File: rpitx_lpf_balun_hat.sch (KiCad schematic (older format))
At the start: 5 parts, among them P1 Conn_02x20_Odd_Even

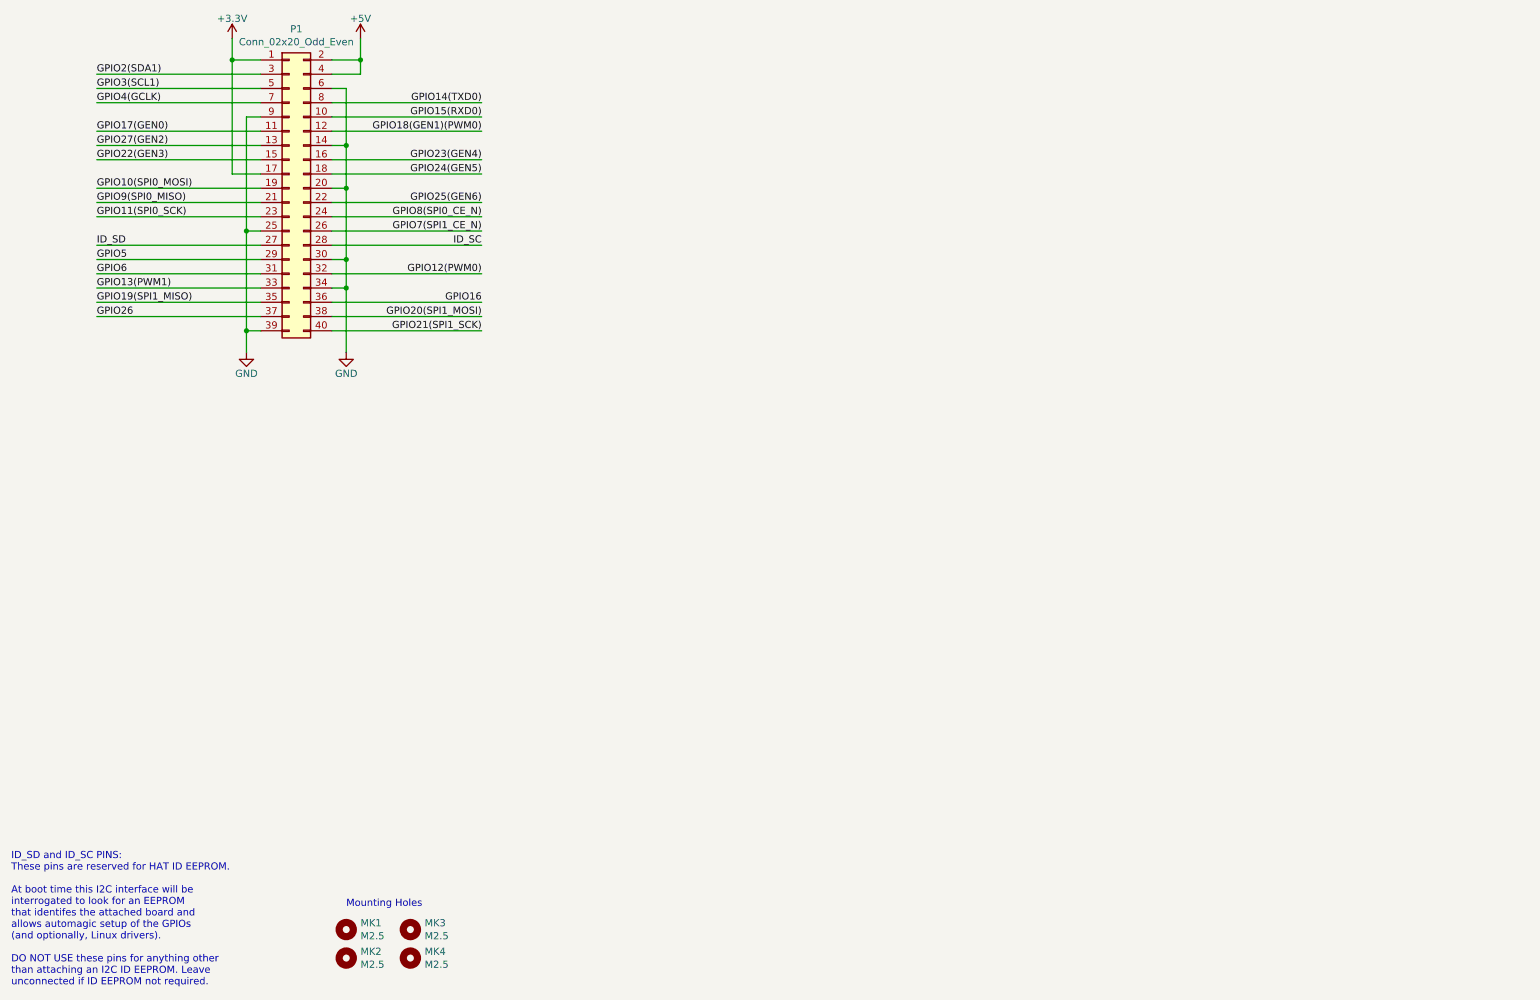
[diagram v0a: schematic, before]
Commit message: 5th order Chebyshev low-pass + balun
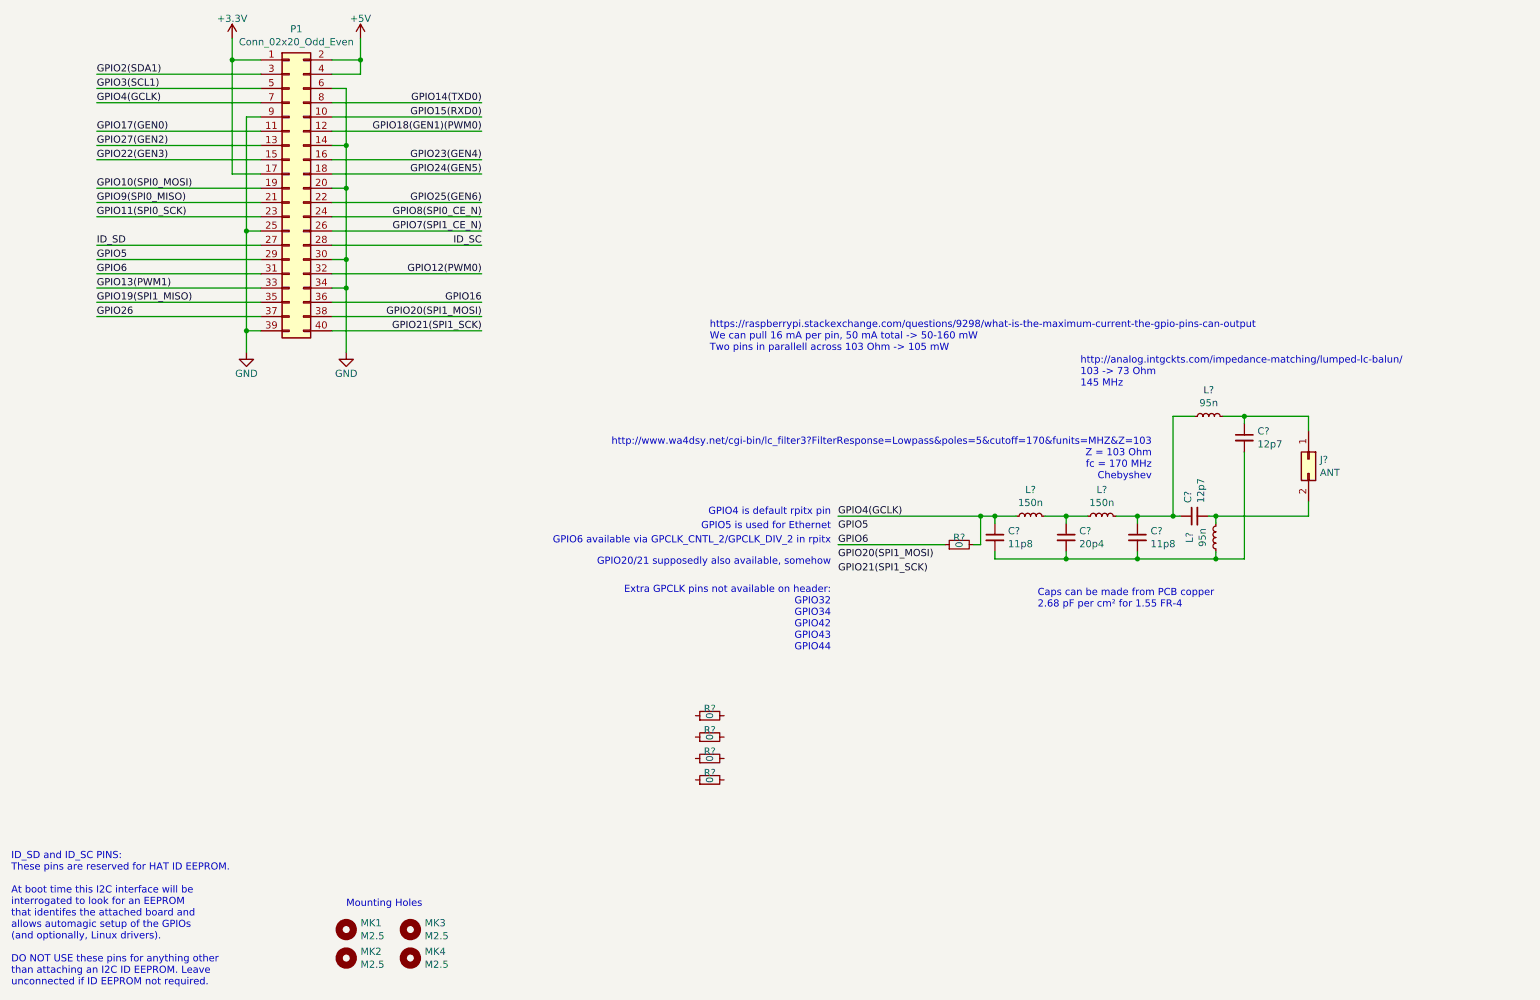
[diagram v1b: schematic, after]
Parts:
- added C? (x2): 11p8, symbol Device:C_Small
- added C?: 20p4, symbol Device:C_Small
- added C? (x2): 12p7, symbol Device:C_Small
- added J?: ANT, symbol Connector_Generic:Conn_02x01
- added L? (x2): 150n, symbol Device:L_Small
- added L? (x2): 95n, symbol Device:L_Small
- added R? (x5): 0, symbol Device:R_Small
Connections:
- net GPIO4(GCLK): now also C?.1, L?.1, R?.2
- net GPIO6: now also R?.1
- new net: C?.1, L?.1, L?.2
- new net: C?.2, C?.2, C?.2, C?.2, L?.1
- new net: C?.1, C?.1, L?.1, L?.2
- new net: C?.1, J?.1 (Pin_1), L?.2
- new net: C?.2, J?.2 (Pin_2), L?.2
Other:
- note added: "Caps can be made from PCB copper\n2.68 pF per cm² for 1.55 FR-4"
- note added: "Extra GPCLK pins not available on header:\nGPIO32\nGPIO34\nGPIO42\nGPIO43\nGPIO44"
- note added: "GPIO20/21 supposedly also available, somehow"
- note added: "GPIO4 is default rpitx pin"
- note added: "GPIO5 is used for Ethernet"
- note added: "GPIO6 available via GPCLK_CNTL_2/GPCLK_DIV_2 in rpitx"
- note added: "http://analog.intgckts.com/impedance-matching/lumped-lc-balun/\n103 -> 73 Ohm\n145 MHz"
- note added: "http://www.wa4dsy.net/cgi-bin/lc_filter3?FilterResponse=Lowpass&poles=5&cutoff=170&funits=MHZ&Z=103\nZ = 103 Ohm\nfc = 170 MHz\nChebyshev"
- note added: "https://raspberrypi.stackexchange.com/questions/9298/what-is-the-maximum-current-the-gpio-pins-can-output\nWe can pull 16 mA per pin, 50 mA total -> 50-160 mW\nTwo pins in parallell across 103 Ohm -> 105 mW"

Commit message: Add second 206 Ohm path
This way we don't have to mess around with rpitx to get GPIO6 output
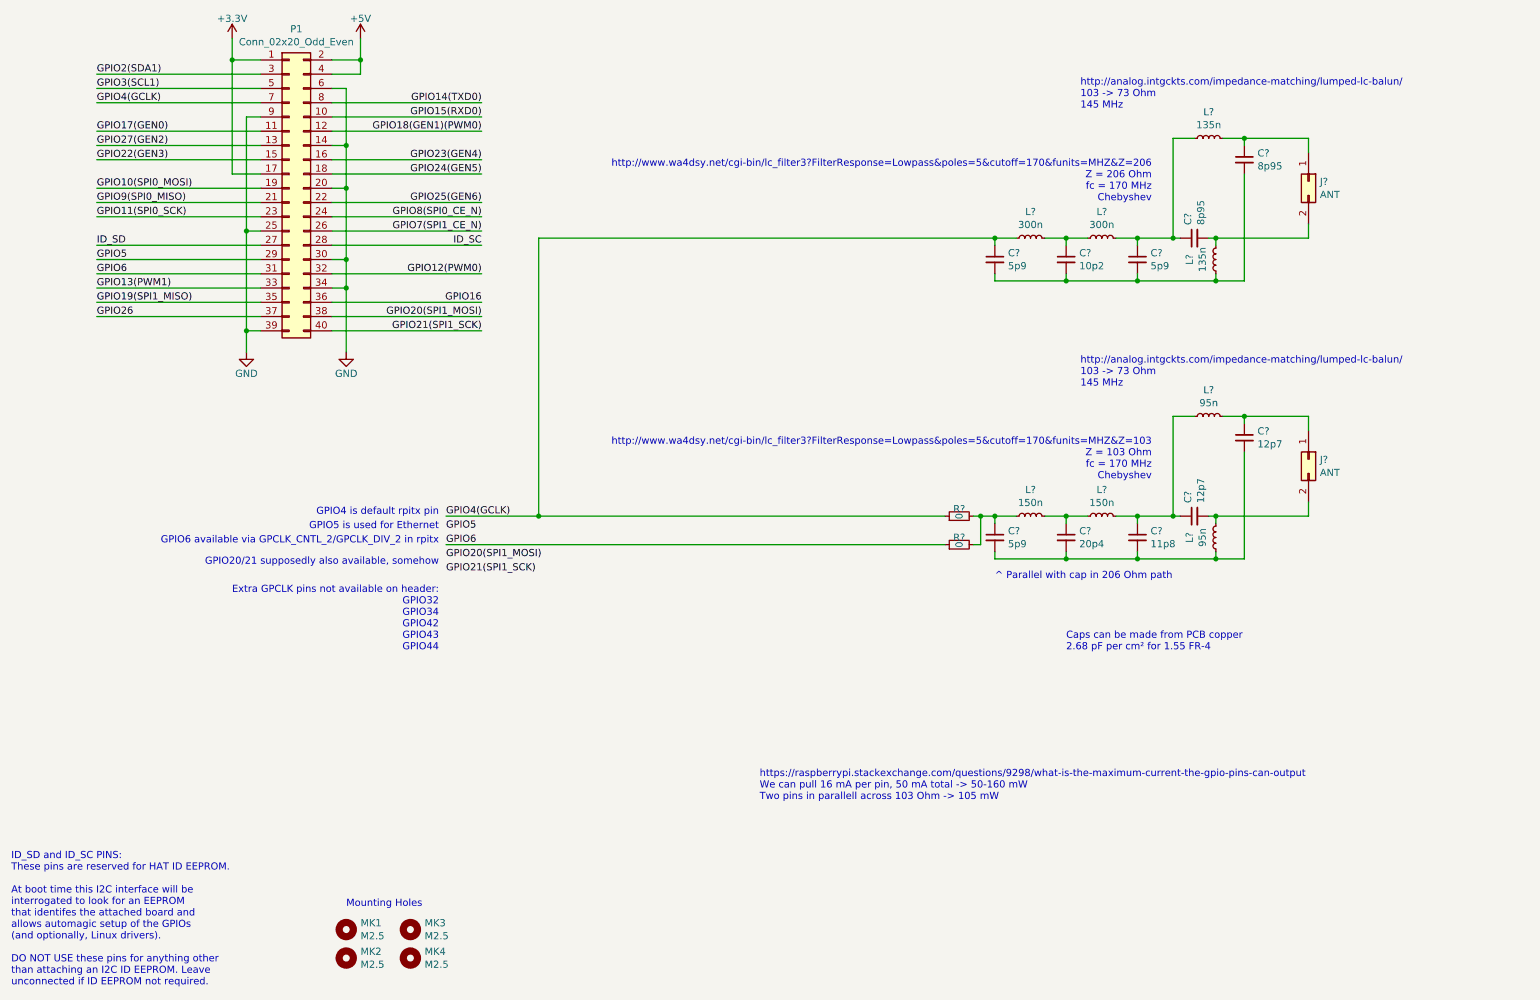
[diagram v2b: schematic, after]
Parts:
- removed R? (x4): 0, symbol Device:R_Small
- added C? (x2): 5p9, symbol Device:C_Small
- added C?: 10p2, symbol Device:C_Small
- added C? (x2): 8p95, symbol Device:C_Small
- added J?: ANT, symbol Connector_Generic:Conn_02x01
- added L? (x2): 300n, symbol Device:L_Small
- added L? (x2): 135n, symbol Device:L_Small
- added R?: 0, symbol Device:R_Small
- C?: value 11p8 -> 5p9
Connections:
- net GPIO4(GCLK): now also C?.1, L?.1, R?.1; no longer C?.1, L?.1, R?.2
- new net: C?.1, L?.1, R?.2, R?.2
- new net: C?.1, L?.1, L?.2
- new net: C?.2, C?.2, C?.2, C?.2, L?.1
- new net: C?.1, C?.1, L?.1, L?.2
- new net: C?.1, J?.1 (Pin_1), L?.2
- new net: C?.2, J?.2 (Pin_2), L?.2
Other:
- note added: "^ Parallel with cap in 206 Ohm path"
- note added: "http://www.wa4dsy.net/cgi-bin/lc_filter3?FilterResponse=Lowpass&poles=5&cutoff=170&funits=MHZ&Z=206\nZ = 206 Ohm\nfc = 170 MHz\nChebyshev"

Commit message: Only 206 Ohm circuit, add thing to solder antenna to
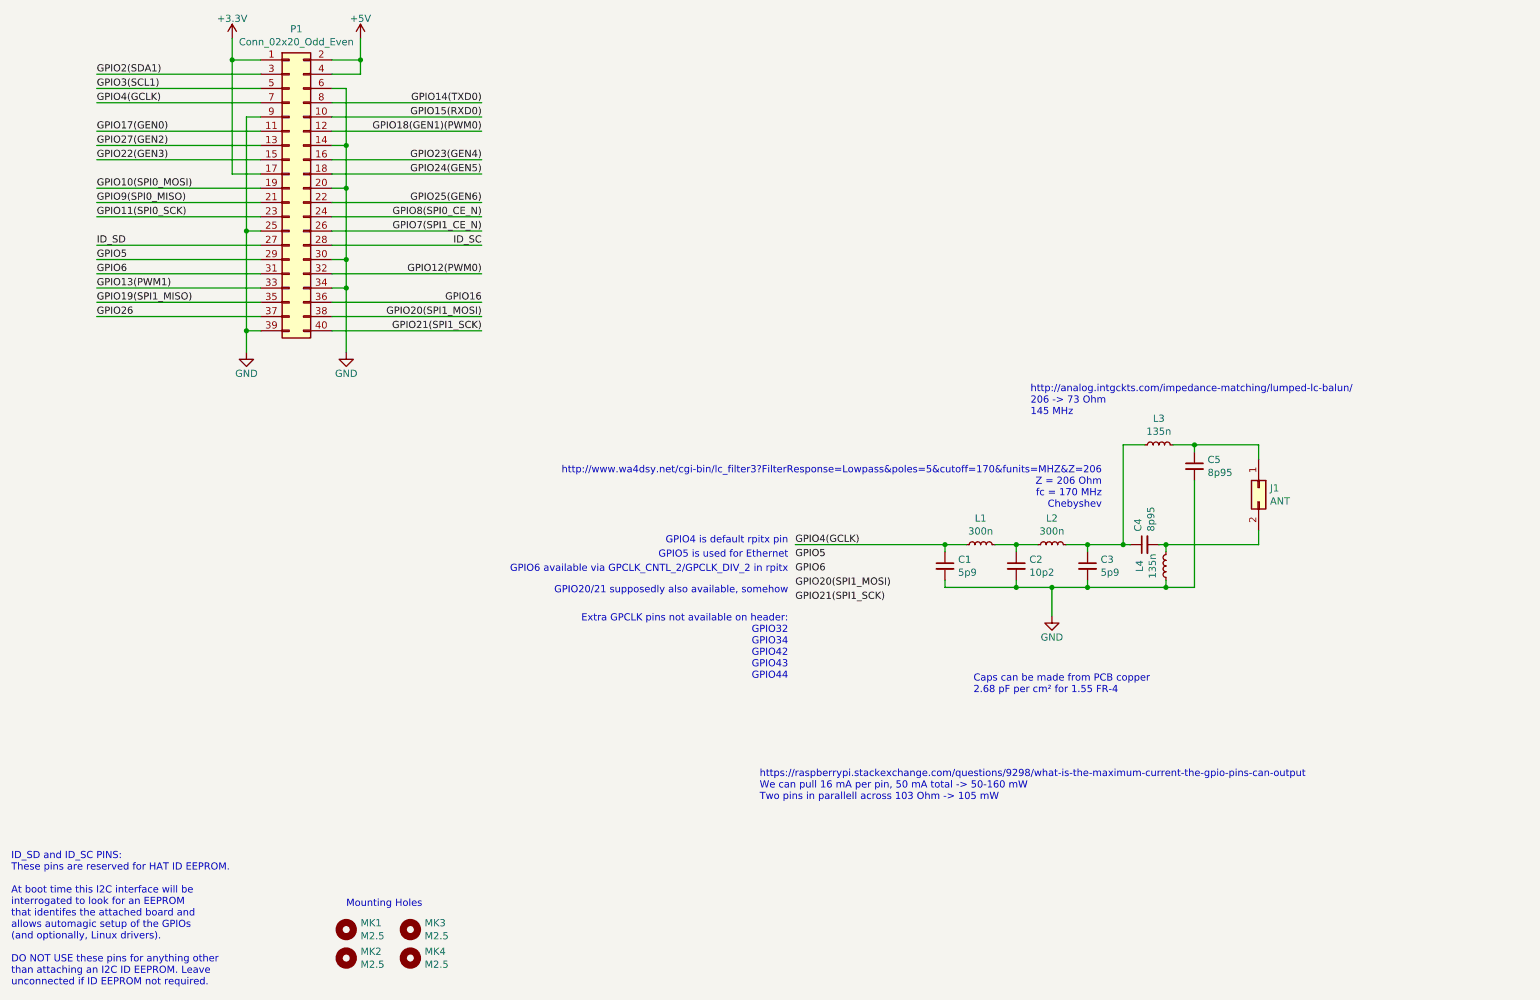
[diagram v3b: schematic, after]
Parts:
- removed C?: 5p9, symbol Device:C_Small
- removed C?: 20p4, symbol Device:C_Small
- removed C?: 11p8, symbol Device:C_Small
- removed C? (x2): 12p7, symbol Device:C_Small
- removed J?: ANT, symbol Connector_Generic:Conn_02x01
- removed L? (x2): 150n, symbol Device:L_Small
- removed L? (x2): 95n, symbol Device:L_Small
- removed R? (x2): 0, symbol Device:R_Small
- C1, C2, C3, C4, C5: renamed from C?; footprint (none) -> Capacitor_SMD:C_0805_2012Metric
- L1, L2, L3, L4: renamed from L?; footprint (none) -> Inductor_SMD:L_0805_2012Metric
- gave numbers to parts that had none: 1
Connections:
- net GND: now also C1.2, C2.2, C3.2, C5.2, L4.1
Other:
- note added: "http://analog.intgckts.com/impedance-matching/lumped-lc-balun/\n206 -> 73 Ohm\n145 MHz"
- note removed: "^ Parallel with cap in 206 Ohm path"
- note removed: "http://analog.intgckts.com/impedance-matching/lumped-lc-balun/\n103 -> 73 Ohm\n145 MHz"
- note removed: "http://www.wa4dsy.net/cgi-bin/lc_filter3?FilterResponse=Lowpass&poles=5&cutoff=170&funits=MHZ&Z=103\nZ = 103 Ohm\nfc = 170 MHz\nChebyshev"
- moved on the sheet: C1, C2, C3, C4, C5, J1, L1, L2, L3, L4

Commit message: Hook footprint lib up
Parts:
- J1: footprint (none) -> rpitx_lpf_balun_hat:rpitx_ant
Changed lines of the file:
@@
 F 0 "J1" V 9404 4180 50  0000 L CNN
 F 1 "ANT" V 9495 4180 50  0000 L CNN
-F 2 "" H 9400 4100 50  0001 C CNN
+F 2 "rpitx_lpf_balun_hat:rpitx_ant" H 9400 4100 50  0001 C CNN
 F 3 "~" H 9400 4100 50  0001 C CNN
 	1    9400 4100
